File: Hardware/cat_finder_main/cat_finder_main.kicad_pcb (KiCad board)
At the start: 2 copper layers, 85 x 70 mm, 37 parts, among them J1 BATT, J10 Analog, J11 Bast Pin, J2 BME280, J3 CSS811, J4 DRIVERS, J5 GY-87, J6 PROG, J7 FTDI, J8 Digital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

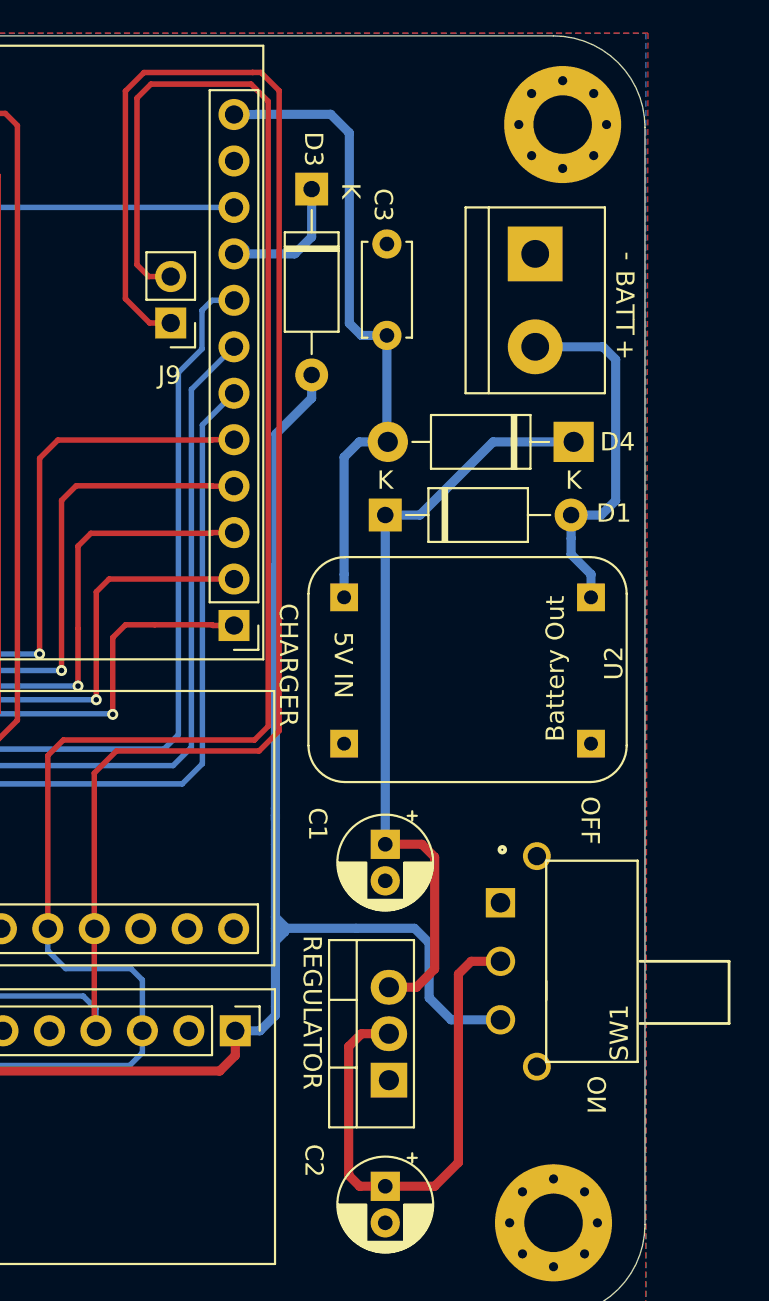
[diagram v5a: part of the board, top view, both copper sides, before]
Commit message: Add MOSFET
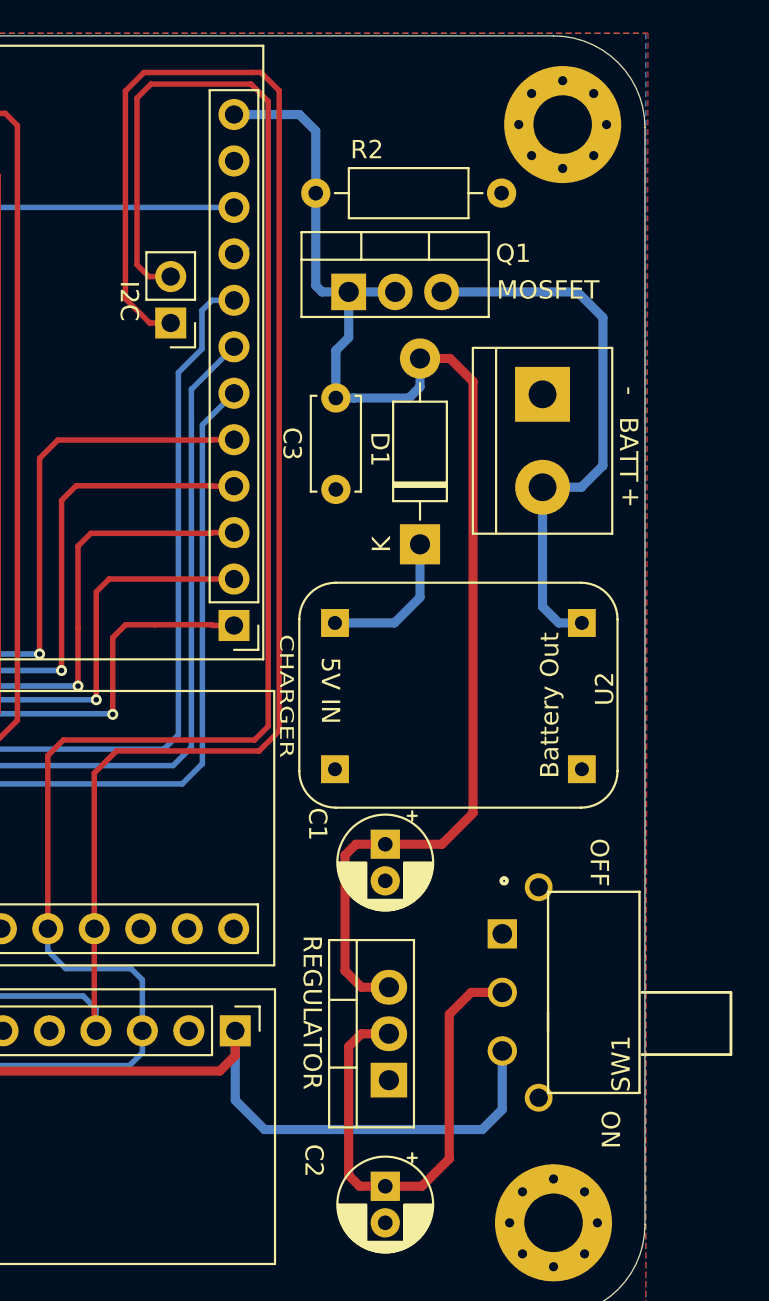
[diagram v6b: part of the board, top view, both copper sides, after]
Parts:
- removed D3: D_Schottky, Diode_THT:D_A-405_P10.16mm_Horizontal
- removed D4: D_Schottky, Diode_THT:D_DO-41_SOD81_P10.16mm_Horizontal
- added Q1: Q_PMOS_GDS, Package_TO_SOT_THT:TO-220-3_Vertical, F.Cu at (168.8, 74.1)
- added R2: 47k, Resistor_THT:R_Axial_DIN0207_L6.3mm_D2.5mm_P10.16mm_Horizontal, F.Cu at (167.0, 68.7)
- D1: value D_Schottky -> 1N5817; footprint Diode_THT:D_A-405_P10.16mm_Horizontal -> Diode_THT:D_DO-41_SOD81_P10.16mm_Horizontal
- moved J1 7.69 mm to (179.4, 79.7)
- moved C3 4.41 mm to (168.1, 79.9), turned to 270 degrees
- moved D1 2.48 mm to (172.7, 87.9), turned to 90 degrees
- moved SW1 1.70 mm to (177.2, 109.2)
- moved U2 1.49 mm to (174.8, 96.2)
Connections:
- C1 pad 1: Net-(C1-Pad1) -> VCC
- D1 pad 1: Net-(C1-Pad1) -> Net-(D1-Pad1)
- D1 pad 2: /BATT -> VCC
- U1 pad 3: Net-(C1-Pad1) -> VCC
- U2 pad 1: VCC -> Net-(D1-Pad1)
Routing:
- net Net-(C1-Pad1): track 42.0 -> 0.00 mm
- net VCC: track 35.7 -> 74.3 mm
- net +3V3: track 182.4 -> 147.9 mm
- net /BATT: track 20.1 -> 30.3 mm
- net Net-(D1-Pad1): track 0.00 -> 8.13 mm
- net Net-(J10-Pad9): track 7.54 -> 0.29 mm
- net Net-(C2-Pad1): track 29.2 -> 27.2 mm
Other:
- board text added: "D1"
- board text added: "I2C"
- board text added: "MOSFET"
- board text removed: "D3"
- board text removed: "K"
